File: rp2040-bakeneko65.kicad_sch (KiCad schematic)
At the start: 33 parts, among them J1 SM04B-SRSS-TB, J2 SWD, SW85 SW_Push, U1 RP2040, U2 W25Q128JVS, U3 XC6206PxxxMR, U4 SRV05, Y1 12MHz

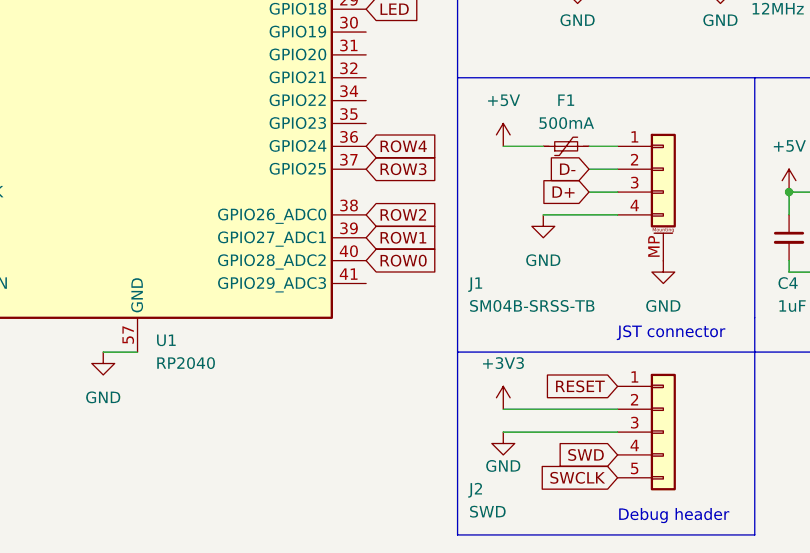
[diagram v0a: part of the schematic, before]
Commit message: oops, have to connect col0 as well
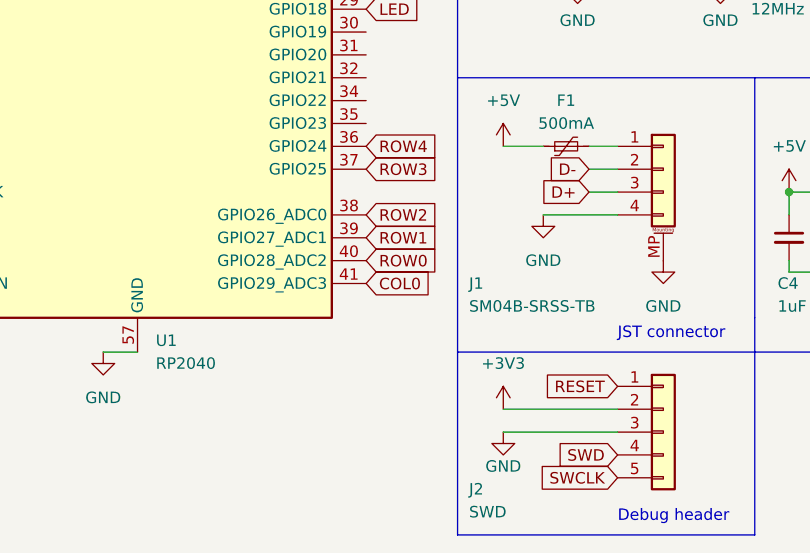
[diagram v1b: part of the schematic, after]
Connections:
- net COL0: now reaches U1.41 (GPIO29_ADC3)
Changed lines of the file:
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@@
+    )
+  )
+  (global_label "COL0" (shape input) (at 97.79 105.41 0) (fields_autoplaced)
+    (effects (font (size 1.27 1.27)) (justify left))
+    (property "Intersheetrefs" "${INTERSHEET_REFS}" (at 105.5339 105.41 0)
+      (effects (font (size 1.27 1.27)) (justify left) hide)
     )
   )

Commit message: JLC tools + C9 needed a bigger footprint
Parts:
- C9: footprint Capacitor_SMD:C_0402_1005Metric -> Capacitor_SMD:C_0603_1608Metric
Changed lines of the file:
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@@
       (effects (font (size 1.27 1.27)) (justify left))
     )
-    (property "Footprint" "Capacitor_SMD:C_0402_1005Metric" (at 182.88 50.8 0)
+    (property "Footprint" "Capacitor_SMD:C_0603_1608Metric" (at 182.88 50.8 0)
       (effects (font (size 1.27 1.27)) hide)
     )

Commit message: some BOM stuff
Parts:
- LED1: value MX_SK6812MINI-E -> WS2812B
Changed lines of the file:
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@@
       (effects (font (size 1.27 1.27)))
     )
-    (property "Value" "MX_SK6812MINI-E" (at 270.51 30.48 0)
+    (property "Value" "WS2812B" (at 265.43 30.48 0)
       (effects (font (size 1.27 1.27)))
     )

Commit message: make fuse smaller
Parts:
- F1: footprint Fuse:Fuse_1206_3216Metric -> Fuse:Fuse_0805_2012Metric
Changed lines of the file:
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@@
       (effects (font (size 1.27 1.27)))
     )
-    (property "Footprint" "Fuse:Fuse_1206_3216Metric" (at 125.095 88.9 0)
+    (property "Footprint" "Fuse:Fuse_0805_2012Metric" (at 125.095 88.9 0)
       (effects (font (size 1.27 1.27)) (justify left) hide)
     )

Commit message: changing to a 4.7uF bulk cap
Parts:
- C9: value 10uF -> 4.7uF
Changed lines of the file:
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@@
       (effects (font (size 1.27 1.27)) (justify left))
     )
-    (property "Value" "10uF" (at 185.42 53.34 0)
+    (property "Value" "4.7uF" (at 185.42 53.34 0)
       (effects (font (size 1.27 1.27)) (justify left))
     )

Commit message: change bulk cap to 0402 again
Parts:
- C9: footprint Capacitor_SMD:C_0603_1608Metric -> Capacitor_SMD:C_0402_1005Metric
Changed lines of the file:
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@@
       (effects (font (size 1.27 1.27)) (justify left))
     )
-    (property "Footprint" "Capacitor_SMD:C_0603_1608Metric" (at 182.88 50.8 0)
+    (property "Footprint" "Capacitor_SMD:C_0402_1005Metric" (at 182.88 50.8 0)
       (effects (font (size 1.27 1.27)) hide)
     )

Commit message: oops, forgot to update LED
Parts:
- LED1: value WS2812B -> SK6812 Mini-E; footprint marbastlib-mx:LED_MX_6028R -> PCM_marbastlib-mx:LED_MX_6028R
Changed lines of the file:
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@@
       (effects (font (size 1.27 1.27)))
     )
-    (property "Value" "WS2812B" (at 265.43 30.48 0)
+    (property "Value" "SK6812 Mini-E" (at 269.24 30.48 0)
       (effects (font (size 1.27 1.27)))
     )
-    (property "Footprint" "marbastlib-mx:LED_MX_6028R" (at 255.27 24.765 0)
+    (property "Footprint" "PCM_marbastlib-mx:LED_MX_6028R" (at 255.27 24.765 0)
       (effects (font (size 1.27 1.27)) hide)
     )
